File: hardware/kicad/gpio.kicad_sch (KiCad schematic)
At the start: 5 parts, among them J1 CONN_02X20, J2 CONN_02X20, U1 LFE5U-85F-6BG381C

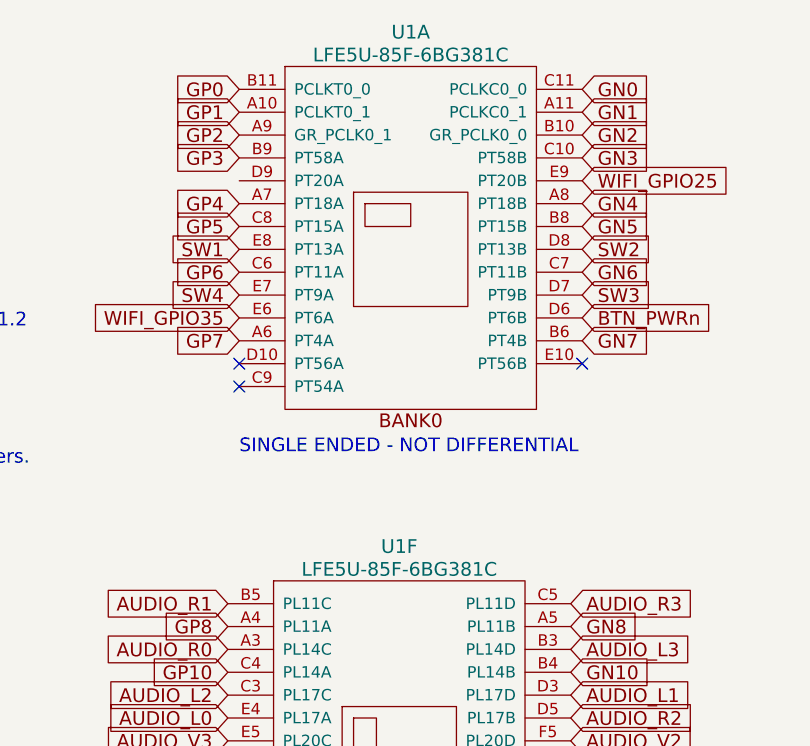
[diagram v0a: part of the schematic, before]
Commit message: Updates FPGA model in BOM and schematics
Replaces LFE5U-25F-6BG381C with LFE5U-85F-8BG381I in multiple files.
Ensures consistency across BOM, schematics, and PCB layouts for the updated FPGA model.
Adjusts related properties such as part number and connectivity attributes.

Addresses a hardware specification upgrade in branch 1.1.
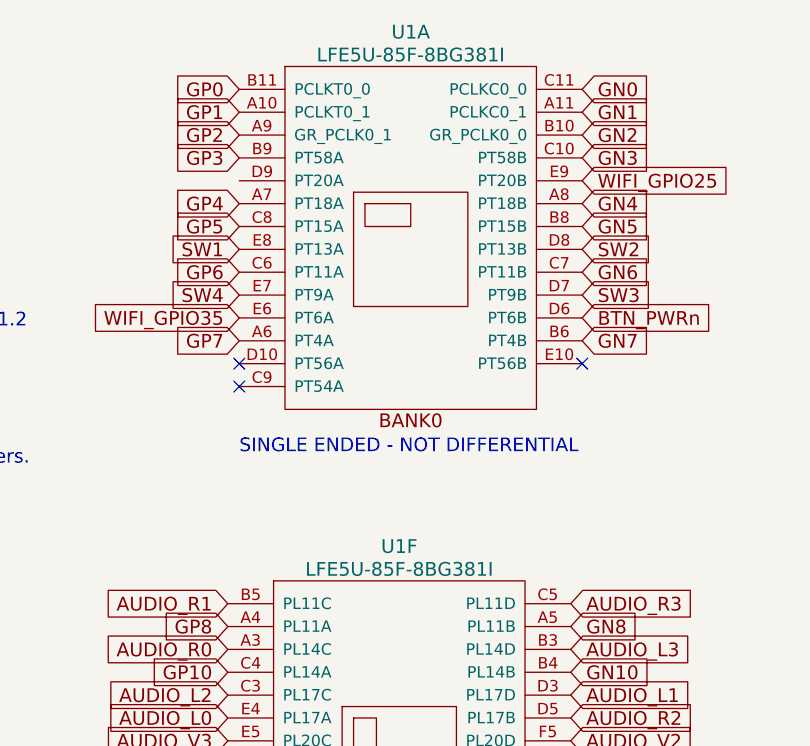
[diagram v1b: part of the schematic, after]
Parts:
- U1: value LFE5U-85F-6BG381C -> LFE5U-85F-8BG381I; MPN LFE5U-85F-6BG381C -> LFE5U-85F-8BG381I
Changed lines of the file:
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@@
 			)
 		)
-		(property "Value" "LFE5U-85F-6BG381C"
+		(property "Value" "LFE5U-85F-8BG381I"
 			(at 134.62 36.83 0)
 			(effects
@@
 			)
 		)
-		(property "MPN" "LFE5U-85F-6BG381C"
+		(property "MPN" "LFE5U-85F-8BG381I"
 			(at 134.62 58.42 0)
 			(effects
@@
 			)
 		)
-		(property "Value" "LFE5U-85F-6BG381C"
+		(property "Value" "LFE5U-85F-8BG381I"
 			(at 133.35 93.98 0)
 			(effects
@@
 			)
 		)
-		(property "MPN" "LFE5U-85F-6BG381C"
+		(property "MPN" "LFE5U-85F-8BG381I"
 			(at 133.35 115.57 0)
 			(effects
